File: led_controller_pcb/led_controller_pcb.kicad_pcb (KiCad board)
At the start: 2 copper layers, 50 x 100 mm, 101 parts, among them J1 DCDC, J10 PASSIVE_OUT, J11 VPP, J12 OUT, J13 VPP, J14 OUT, J15 VPP, J16 PASSIVE_OUT, J17 VPP, J18 OUT, J19 VPP, J2 DEBUG, J20 OUT, J21 HV_IN_LIVE, J22 HV_IN_NEUT, J23 PSU_VOUT_LOW, J24 HV_LINE, J25 HV_OUT, J26 HV_LINE, J27 HV_OUT, J28 PSU_LIVE, J29 PSU_NEUT, J3 VPP, J31 PSU_GND, J32 PSU_VOUT, J4 PASSIVE_OUT, J5 VPP, J6 OUT, J7 VPP, J8 OUT, J9 VPP, Q1 IRF540N, Q10 BT136-600, Q2 IRF540N, Q3 IRF540N, Q4 IRF540N, Q5 IRF540N, Q6 IRF540N, Q7 BC549, Q8 BC549, Q9 BT136-600, SW1 BUTTON, SW2 BUTTON, U1 ESP-12E, U2 TC4427A, U3 TC4427A, U4 TC4427A, U5 STM32F030F4Px, U6 MOC3023M, U7 MOC3023M, U8 H11AA1, Y1 8MHz

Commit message: minor changes
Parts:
- REF** (x4): value MountingHole_3.2mm_M3 -> MountingHole_3.2mm_M3_Pad; footprint MountingHole:MountingHole_3.2mm_M3 -> MountingHole:MountingHole_3.2mm_M3_Pad

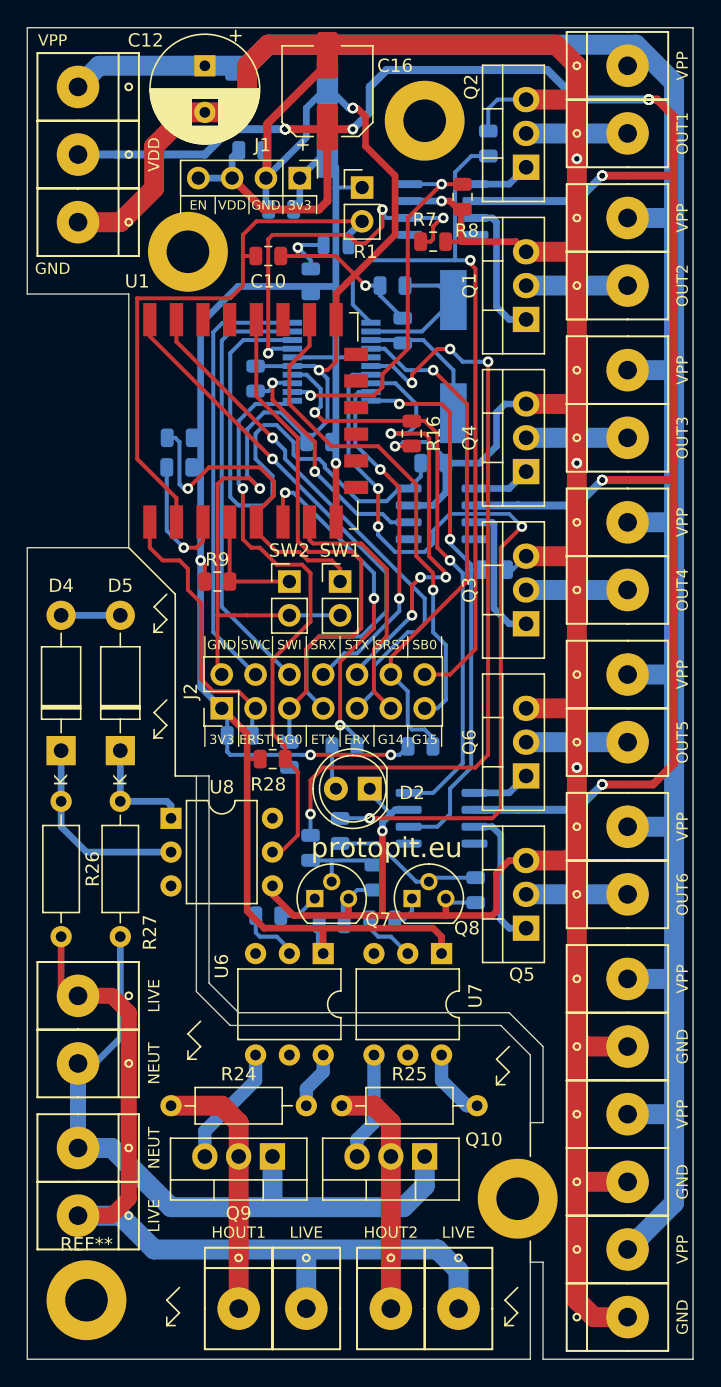
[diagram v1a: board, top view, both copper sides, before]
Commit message: update 0805 components to have larger pads
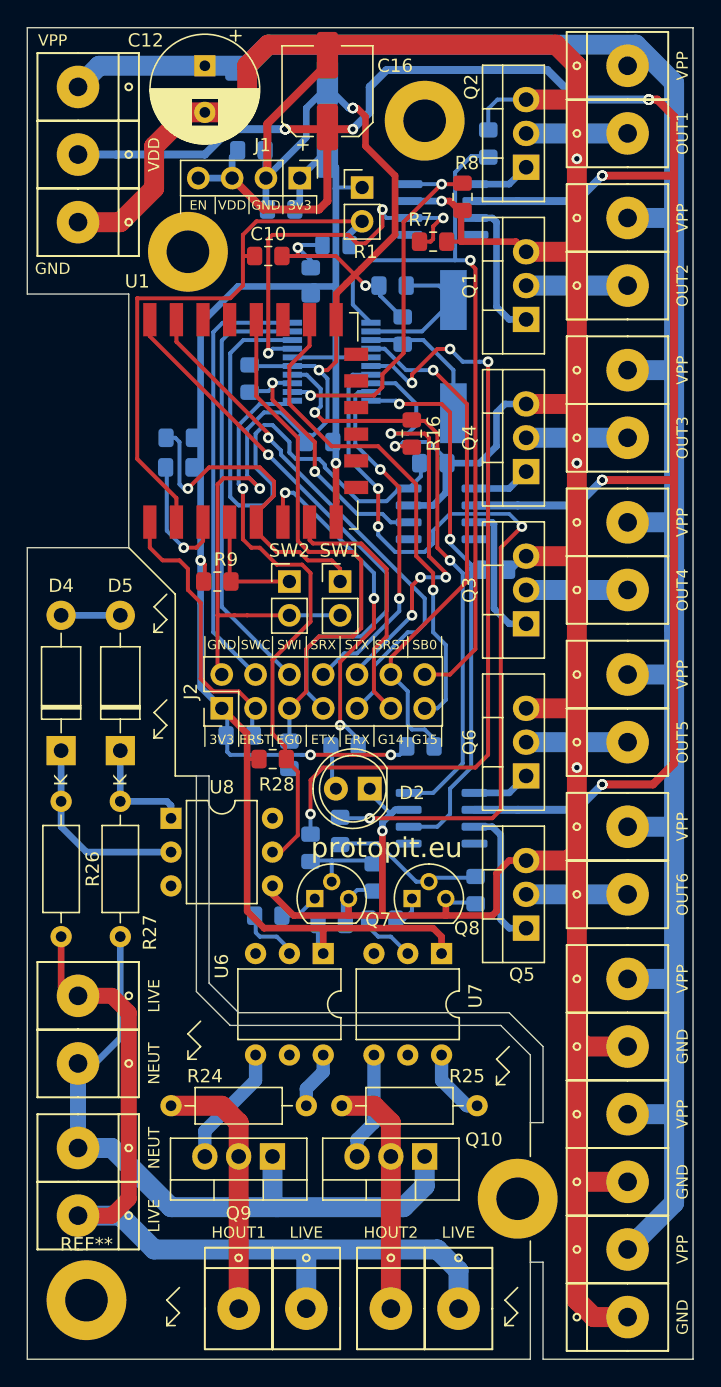
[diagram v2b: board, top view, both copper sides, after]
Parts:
- C1, C10, C11, C13, C14, C15, C2, C4, C5, C6, C7, C9: footprint Capacitor_SMD:C_0805_2012Metric -> Capacitor_SMD:C_0805_2012Metric_Pad1.15x1.40mm_HandSolder
- R10, R11, R12, R13, R14, R15, R16, R18, R19, R2, R20, R21, R22, R23, R28, R3, R4, R5, R6, R7, R8, R9: footprint Resistor_SMD:R_0805_2012Metric -> Resistor_SMD:R_0805_2012Metric_Pad1.15x1.40mm_HandSolder
- moved R12 0.44 mm to (134.2, 78.7)

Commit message: update kicad files
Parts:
- moved C7 1.73 mm to (136.0, 61.5)
- moved C11 0.62 mm to (133.0, 56.2)
- moved REF** 0.54 mm to (121.9, 148.5)
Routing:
- net GND: track 383.3 -> 206.3 mm
- net VPP: track 160.9 -> 0.00 mm
- net /GPO2: track 62.2 -> 61.0 mm
- net VDD: track 165.2 -> 166.0 mm
- added copper zone on F.Cu, net GND
- added copper zone on B.Cu, net VPP

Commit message: update pcb
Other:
- net class Default removed

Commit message: fix stupid pcb mistake
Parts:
- moved C7 4.84 mm to (134.2, 66.0)
- moved C9 1.46 mm to (138.0, 66.0)
- moved C5 0.31 mm to (138.8, 71.8)
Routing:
- net GND: track 206.3 -> 209.3 mm
